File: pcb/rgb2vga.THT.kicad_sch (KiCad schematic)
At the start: 43 parts, among them J1 GPIO_0, J2 RGB_IN, J3 COCO3_RGB_IN, J4 C_VIDEO_IN, J5 GPIO_1, J6 VGA_OUT, J7 Conn_01x03_Male, SW1 SW_DIP_x10, SW2 SW_DP3T, U1 LM1881

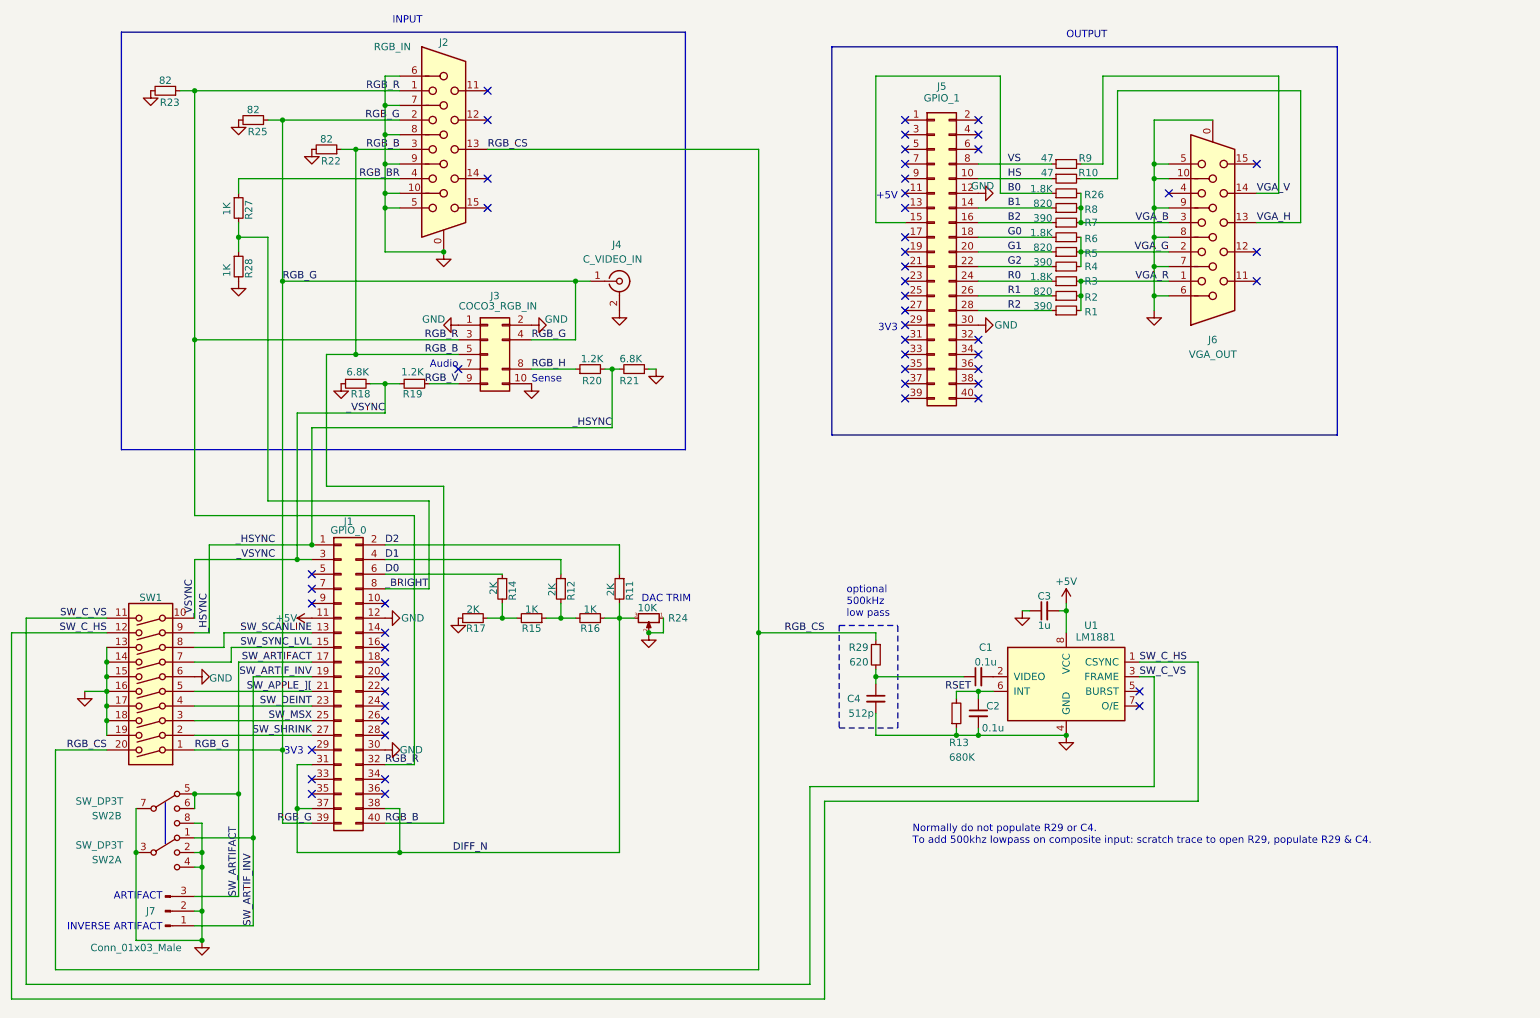
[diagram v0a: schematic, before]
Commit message: SMT passives, add lowpass, decouple lm1881
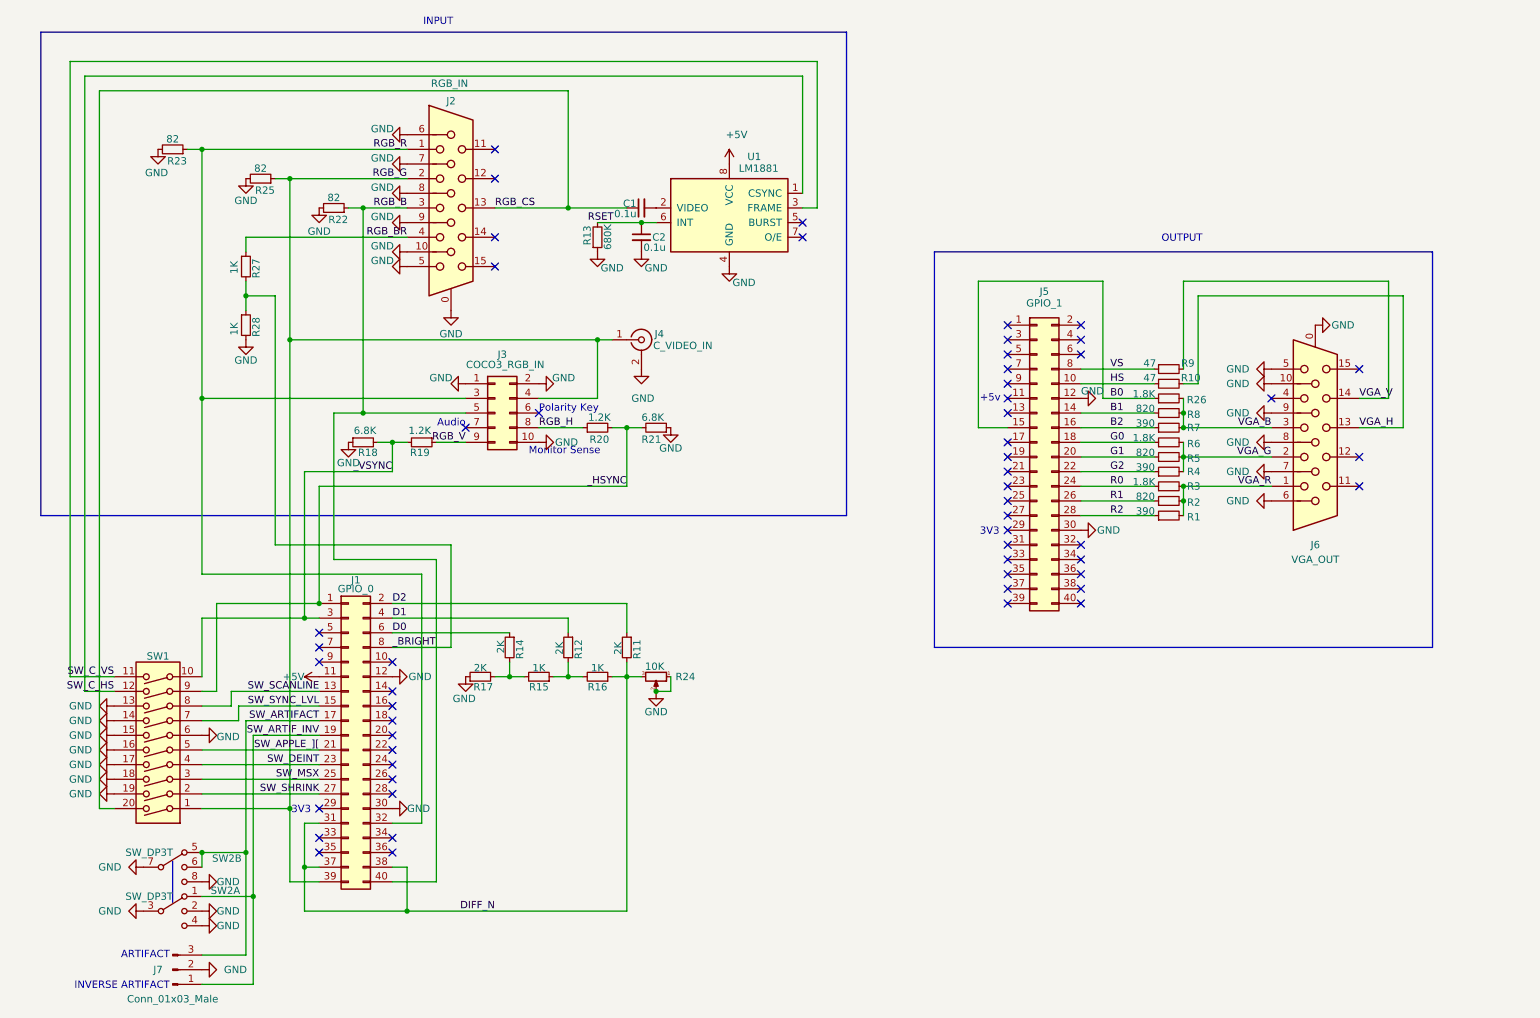
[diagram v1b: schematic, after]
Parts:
- removed C3: 1u, 000_LOCAL:C_0805, symbol 000_LOCAL:C_Small
- removed C4: 512p, 000_LOCAL:C_0805, symbol 000_LOCAL:C_Small
- removed R29: 620, 000_LOCAL:R_0805_SJC, symbol 000_LOCAL:R_Small
- C1, C2: footprint 000_LOCAL:C_0805 -> 000_LOCAL:C025-025X050
- J3: footprint 000_LOCAL:IDC-Header_2x05_P2.54mm_Horizontal COCO3 KEYED -> 000_LOCAL:IDC-Header_2x05_P2.54mm_Horizontal; symbol 000_LOCAL:Conn_02x05_Odd_Even_COCO3_KEYED -> 000_LOCAL:Conn_02x05_Odd_Even
- R1, R10, R11, R12, R13, R14, R15, R16, R17, R18, R19, R2, R20, R21, R22, R23, R25, R26, R27, R28, R3, R4, R5, R6, R7, R8, R9: footprint 000_LOCAL:R_0805 -> 000_LOCAL:0207_10
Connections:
- net RGB_CS: now also C1.1
- no-connect marks 55 -> 56
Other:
- note added: "+5v"
- note added: "Monitor Sense"
- note added: "Polarity Key"
- note removed: "+5V"
- note removed: "DAC TRIM"
- note removed: "Normally do not populate R29 or C4. To add 500khz lowpass on composite input: scratch trace to open R29, populate R29 & C4."
- note removed: "Sense"
- note removed: "optional 500kHz low pass"
- title: DE0-NANO RGB2VGA -> DE0-NANO RGB2VGA THT
- moved on the sheet: C1, C2, J1, J2, J4, J5, J6, J7, R1, R10, R11, R12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
